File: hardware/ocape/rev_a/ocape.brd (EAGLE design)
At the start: 54.6 x 59.9 mm, 9 parts, among them J1 CON_HEADER_2X05-PTH+SHROUDED_A, J2 JUMPER-PTH-2-NO, P9/P8 BBB_HEADERS, U1 CAT24C256WI-GT3

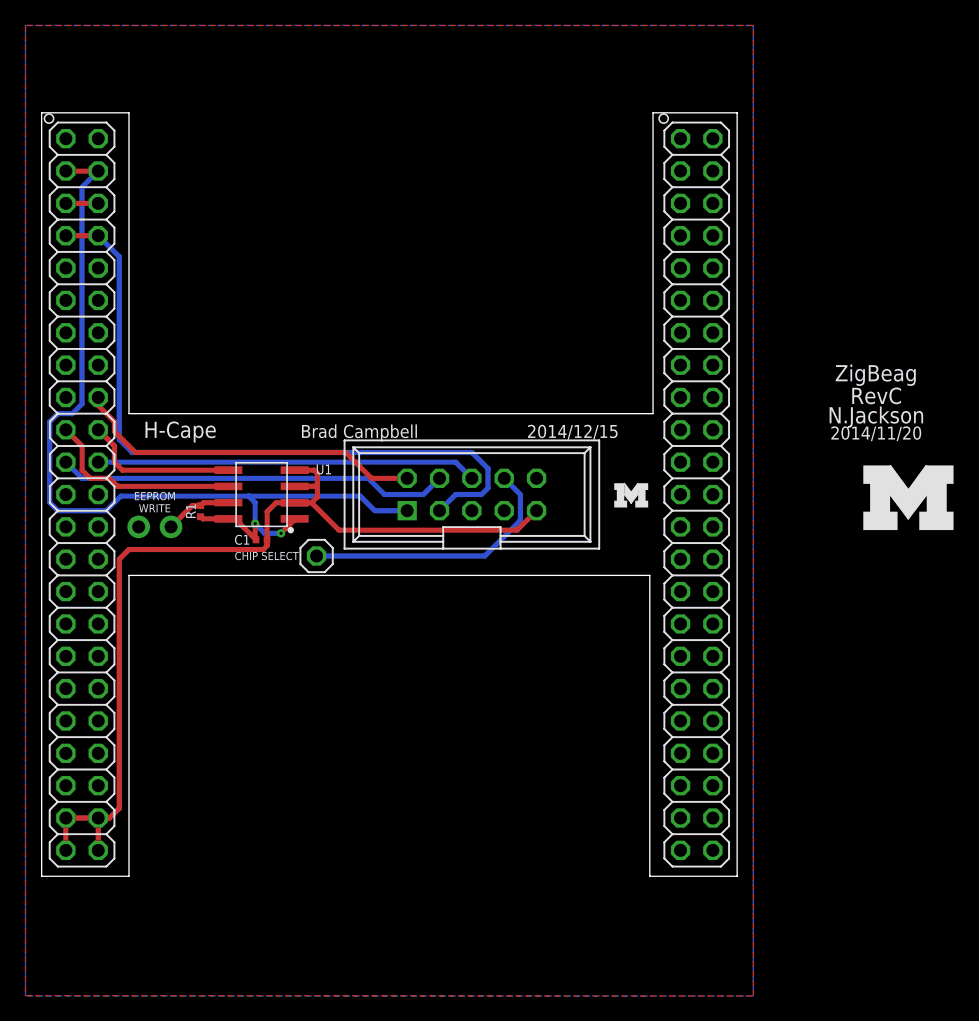
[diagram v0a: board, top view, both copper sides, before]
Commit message: new design with mountable sensor board
If the sensor board doesn't need to be attached elsewhere, it can be
attached to the BBB cape.
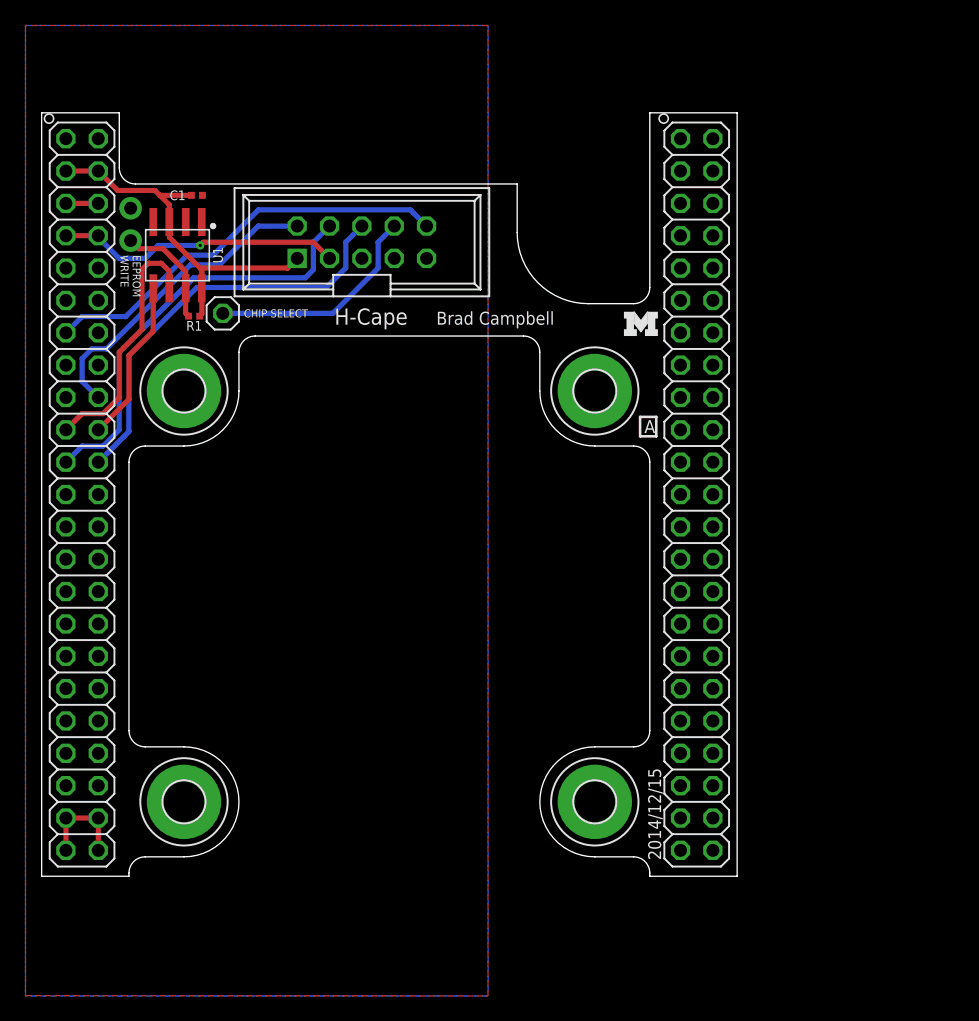
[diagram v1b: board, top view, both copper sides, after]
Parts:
- removed U$2: (no value), logos:UMICH_SOLID_200MIL
- added H5, H6, H7, H8: MOUNT-PAD-ROUND3.2, holes:3,2-PAD
- moved C1 27.5 mm to (12.2, 61.6)
- moved J2 23.8 mm to (6.99, 59.3), turned to 90 degrees
- moved J1 21.6 mm to (25.1, 57.9)
- moved JP1 20.4 mm to (14.2, 52.3)
- moved U1 19.9 mm to (10.7, 56.9), turned to 270 degrees
- moved R1 15.3 mm to (12.0, 52.1), turned to 180 degrees
- moved LOGO1 13.5 mm to (45.7, 50.5)
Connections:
- net GND: now also H5.B3,2, H6.B3,2, H7.B3,2, H8.B3,2, U1.A0; no longer U1.A2
- net OBSERVER_INT: now also P9/P8.P9_13
- net VCC: now also U1.A2; no longer U1.A0
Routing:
- net GND: track 73.1 -> 7.62 mm
- net VCC: track 72.8 -> 29.5 mm, vias 2 -> 0
- net OBSERVER_INT: track 0.00 -> 32.8 mm
- net 5V: track 55.2 -> 22.6 mm, vias 0 -> 1
- net SCL: track 15.7 -> 20.2 mm
- net N$31: track 5.30 -> 8.93 mm
- net !OBSERVER_CS: track 21.0 -> 17.5 mm
- net SCLK: track 29.9 -> 33.1 mm
- net MOSI: track 27.7 -> 24.8 mm
- net MISO: track 30.9 -> 33.2 mm
- net SDA: track 12.3 -> 12.9 mm
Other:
- outline, holes or cut-outs redrawn
- board text added: "A"
- board text removed: "2014/11/20"
- board text removed: "N.Jackson"
- board text removed: "RXD"
- board text removed: "RevC"
- board text removed: "SCL"
- board text removed: "SDA"
- board text removed: "TXD"
- board text removed: "ZigBeag"

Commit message: basically done with observer
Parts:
- renumbered JP1 to J3
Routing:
- net GND: track 7.62 -> 142.7 mm
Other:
- outline, holes or cut-outs redrawn
- board text added: "2014/12/16"
- board text removed: "2014/12/15"

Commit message: shipped rev a
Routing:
- net GND: track 142.7 -> 145.9 mm
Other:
- outline, holes or cut-outs redrawn
- board text removed: "CE1"
